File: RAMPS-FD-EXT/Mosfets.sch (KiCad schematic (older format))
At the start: 30 parts, among them P301 FET_1, P302 FET_0, P303 FET_3, P304 FET_2, Q301 2N7002, Q302 2N7002, Q303 IRLB8743PBF, Q304 IRLB8743PBF, Q305 2N7002, Q306 2N7002, Q307 IRLB8743PBF, Q308 IRLB8743PBF

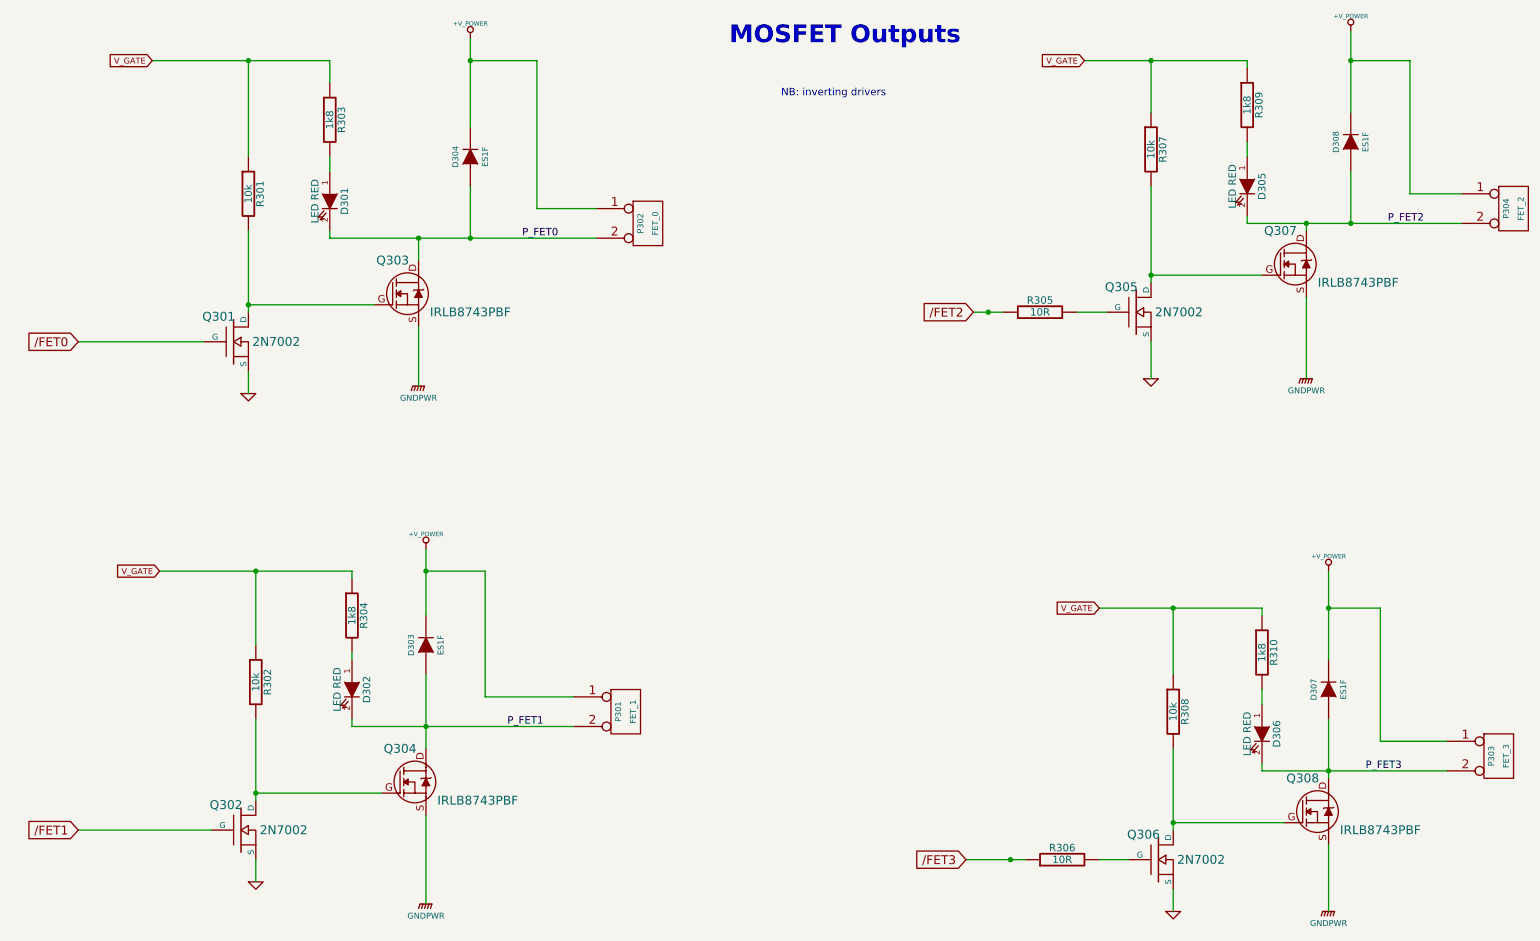
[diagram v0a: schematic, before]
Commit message: EXT4: update schematic, layout
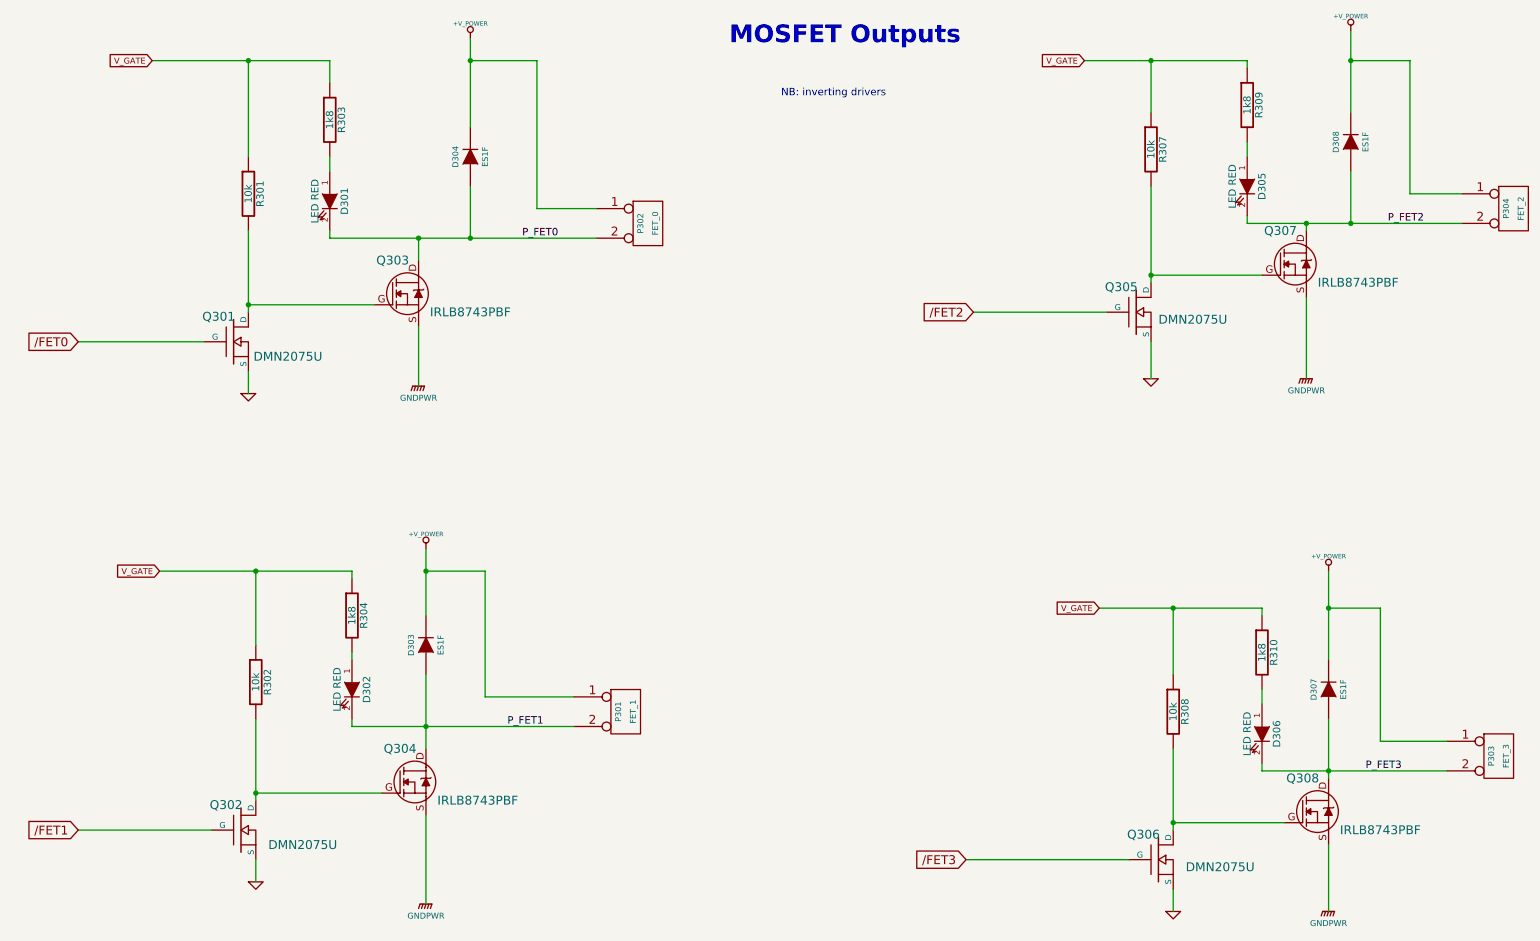
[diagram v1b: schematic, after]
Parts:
- removed R305, R306: 10R, symbol R
- Q301, Q302, Q305, Q306: value 2N7002 -> DMN2075U
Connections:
- net /FET2: now also Q305.G
- net /FET3: now also Q306.G
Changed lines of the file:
@@
 Sheet 3 4
 Title ""
-Date "21 sep 2013"
+Date "26 sep 2013"
 Rev ""
 Comp ""
@@
 $EndDescr
 $Comp
-L GNDPWR #PWR042
+L GNDPWR #PWR046
 U 1 1 523B8B99
 P 3500 3050
-F 0 "#PWR042" H 3500 3100 40  0001 C CNN
+F 0 "#PWR046" H 3500 3100 40  0001 C CNN
 F 1 "GNDPWR" H 3500 2970 40  0000 C CNN
 F 2 "" H 3500 3050 60  0001 C CNN
@@
 $EndComp
 $Comp
-L +V_POWER #PWR043
+L +V_POWER #PWR047
 U 1 1 523B8B8F
 P 3850 700
-F 0 "#PWR043" H 3850 670 30  0001 C CNN
+F 0 "#PWR047" H 3850 670 30  0001 C CNN
 F 1 "+V_POWER" H 3850 800 30  0000 C CNN
 F 2 "" H 3850 700 60  0001 C CNN
@@
 	1    0    0    -1
 $EndComp
-$Comp
-L R R306
-U 1 1 523B8B8A
-P 7850 6250
-F 0 "R306" V 7930 6250 50  0000 C CNN
-F 1 "10R" V 7850 6250 50  0000 C CNN
-F 2 "" H 7850 6250 60  0001 C CNN
-F 3 "" H 7850 6250 60  0001 C CNN
-	1    7850 6250
-	0    -1   -1   0
-$EndComp
 Text GLabel 1200 6050 0    60   Input ~ 0
 /FET1
@@
 P 8500 6250
 F 0 "Q306" H 8510 6420 60  0000 R CNN
-F 1 "2N7002" H 8950 6250 60  0000 R CNN
+F 1 "DMN2075U" H 9150 6200 60  0000 R CNN
 F 2 "" H 8500 6250 60  0001 C CNN
 F 3 "" H 8500 6250 60  0001 C CNN
@@
 $EndComp
 $Comp
-L +V_POWER #PWR044
+L +V_POWER #PWR048
 U 1 1 523B8B82
 P 9650 4300
-F 0 "#PWR044" H 9650 4270 30  0001 C CNN
+F 0 "#PWR048" H 9650 4270 30  0001 C CNN
 F 1 "+V_POWER" H 9650 4400 30  0000 C CNN
 F 2 "" H 9650 4300 60  0001 C CNN
@@
 $EndComp
 $Comp
-L +V_POWER #PWR045
+L +V_POWER #PWR049
 U 1 1 523B8B81
 P 3550 4150
-F 0 "#PWR045" H 3550 4120 30  0001 C CNN
+F 0 "#PWR049" H 3550 4120 30  0001 C CNN
 F 1 "+V_POWER" H 3550 4250 30  0000 C CNN
 F 2 "" H 3550 4150 60  0001 C CNN
@@
 $EndComp
 $Comp
-L +V_POWER #PWR046
+L +V_POWER #PWR050
 U 1 1 523B8B7F
 P 9800 650
-F 0 "#PWR046" H 9800 620 30  0001 C CNN
+F 0 "#PWR050" H 9800 620 30  0001 C CNN
 F 1 "+V_POWER" H 9800 750 30  0000 C CNN
 F 2 "" H 9800 650 60  0001 C CNN
@@
 P 8350 2550
 F 0 "Q305" H 8360 2720 60  0000 R CNN
-F 1 "2N7002" H 8800 2550 60  0000 R CNN
+F 1 "DMN2075U" H 8500 2500 60  0000 L CNN
 F 2 "" H 8350 2550 60  0001 C CNN
 F 3 "" H 8350 2550 60  0001 C CNN
@@
 /FET2
 $Comp
-L R R305
-U 1 1 523B8B7B
-P 7700 2550
-F 0 "R305" V 7780 2550 50  0000 C CNN
-F 1 "10R" V 7700 2550 50  0000 C CNN
-F 2 "" H 7700 2550 60  0001 C CNN
-F 3 "" H 7700 2550 60  0001 C CNN
-	1    7700 2550
-	0    -1   -1   0
-$EndComp
-$Comp
-L GND #PWR047
+L GND #PWR051
 U 1 1 523B8B7A
 P 8450 3000
-F 0 "#PWR047" H 8450 3000 30  0001 C CNN
+F 0 "#PWR051" H 8450 3000 30  0001 C CNN
 F 1 "GND" H 8450 2930 30  0001 C CNN
 F 2 "" H 8450 3000 60  0001 C CNN
@@
 $EndComp
 $Comp
-L GNDPWR #PWR048
+L GNDPWR #PWR052
 U 1 1 523B8B6F
 P 3550 6550
-F 0 "#PWR048" H 3550 6600 40  0001 C CNN
+F 0 "#PWR052" H 3550 6600 40  0001 C CNN
 F 1 "GNDPWR" H 3550 6470 40  0000 C CNN
 F 2 "" H 3550 6550 60  0001 C CNN
@@
 $EndComp
 $Comp
-L GNDPWR #PWR049
+L GNDPWR #PWR053
 U 1 1 523B8B6E
 P 9650 6600
-F 0 "#PWR049" H 9650 6650 40  0001 C CNN
+F 0 "#PWR053" H 9650 6650 40  0001 C CNN
 F 1 "GNDPWR" H 9650 6520 40  0000 C CNN
 F 2 "" H 9650 6600 60  0001 C CNN
@@
 $EndComp
 $Comp
-L GND #PWR050
+L GND #PWR054
 U 1 1 523B8B6D
 P 8600 6600
-F 0 "#PWR050" H 8600 6600 30  0001 C CNN
+F 0 "#PWR054" H 8600 6600 30  0001 C CNN
 F 1 "GND" H 8600 6530 30  0001 C CNN
 F 2 "" H 8600 6600 60  0001 C CNN
@@
 $EndComp
 $Comp
-L GNDPWR #PWR051
+L GNDPWR #PWR055
 U 1 1 523B8B6C
 P 9500 3000
-F 0 "#PWR051" H 9500 3050 40  0001 C CNN
+F 0 "#PWR055" H 9500 3050 40  0001 C CNN
 F 1 "GNDPWR" H 9500 2920 40  0000 C CNN
 F 2 "" H 9500 3000 60  0001 C CNN
@@
 $EndComp
 $Comp
-L GND #PWR052
+L GND #PWR056
 U 1 1 523B8B6B
 P 2400 6400
-F 0 "#PWR052" H 2400 6400 30  0001 C CNN
+F 0 "#PWR056" H 2400 6400 30  0001 C CNN
 F 1 "GND" H 2400 6330 30  0001 C CNN
 F 2 "" H 2400 6400 60  0001 C CNN
@@
 P 2300 6050
 F 0 "Q302" H 2310 6220 60  0000 R CNN
-F 1 "2N7002" H 2750 6050 60  0000 R CNN
+F 1 "DMN2075U" H 2950 5950 60  0000 R CNN
 F 2 "" H 2300 6050 60  0001 C CNN
 F 3 "" H 2300 6050 60  0001 C CNN
@@
 P 2250 2750
 F 0 "Q301" H 2260 2920 60  0000 R CNN
-F 1 "2N7002" H 2700 2750 60  0000 R CNN
+F 1 "DMN2075U" H 2850 2650 60  0000 R CNN
 F 2 "" H 2250 2750 60  0001 C CNN
 F 3 "" H 2250 2750 60  0001 C CNN
@@
 $EndComp
 $Comp
-L GND #PWR053
+L GND #PWR057
 U 1 1 523B8B66
 P 2350 3100
-F 0 "#PWR053" H 2350 3100 30  0001 C CNN
+F 0 "#PWR057" H 2350 3100 30  0001 C CNN
 F 1 "GND" H 2350 3030 30  0001 C CNN
 F 2 "" H 2350 3100 60  0001 C CNN
@@
 V_GATE
 Wire Wire Line
-	3550 4600 3550 4150
+	3550 4150 3550 4600
 Wire Wire Line
 	2100 6050 1200 6050
@@
 	2400 6400 2400 6250
 Wire Wire Line
-	2400 5850 2400 5300
+	2400 5300 2400 5850
 Wire Wire Line
 	3250 5800 2400 5800
@@
 	9200 5650 10450 5650
 Wire Wire Line
-	9200 4600 9200 4550
+	9200 4550 9200 4600
 Wire Wire Line
 	9650 4300 9650 4900
@@
 	3950 5150 4550 5150
 Wire Wire Line
-	3850 1300 3850 700
+	3850 700  3850 1300
 Wire Wire Line
 	1700 850  2900 850
@@
 	2900 2050 4700 2050
 Wire Wire Line
-	3050 4350 3050 4300
+	3050 4300 3050 4350
 Wire Wire Line
 	3550 5000 3550 5500
@@
 Connection ~ 9800 850
 Wire Wire Line
-	9800 1200 9800 650
+	9800 650  9800 1200
 Wire Wire Line
 	10200 1750 10200 850
@@
 	9200 2300 8450 2300
 Wire Wire Line
-	8450 2350 8450 1700
-Wire Wire Line
-	8150 2550 7950 2550
+	8450 1700 8450 2350
+Wire Wire Line
+	8150 2550 7250 2550
 Wire Wire Line
 	9100 1500 9100 1400
-Wire Wire Line
-	7250 2550 7450 2550
 Wire Wire Line
 	8450 1200 8450 850
@@
 	2900 1600 2900 1500
 Wire Wire Line
-	7200 6250 7600 6250
-Wire Wire Line
 	9200 5200 9200 5100
-Wire Wire Line
-	8300 6250 8100 6250
 Wire Wire Line
 	8600 5500 8600 6050
@@
 Wire Wire Line
 	4300 1850 4700 1850
-Connection ~ 7500 6250
-Connection ~ 7350 2550
 Wire Wire Line
 	9800 1600 9800 1950
@@
 	3050 5350 4550 5350
 Wire Wire Line
-	3050 4300 1750 4300
-Wire Wire Line
-	9650 5700 9650 5300
+	1750 4300 3050 4300
+Wire Wire Line
+	9650 5300 9650 5700
 Wire Wire Line
 	10450 5450 10000 5450
@@
 Connection ~ 9650 4550
 Wire Wire Line
-	9200 4550 8100 4550
+	8100 4550 9200 4550
 Connection ~ 8600 4550
 Wire Wire Line
@@
 	3200 2500 2350 2500
 Wire Wire Line
-	2350 2550 2350 2000
+	2350 2000 2350 2550
 Wire Wire Line
 	2350 3100 2350 2950
@@
 Text Label 9900 5650 0    50   ~ 0
 P_FET3
+Wire Wire Line
+	8300 6250 7200 6250
 $EndSCHEMATC

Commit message: RAMPS-FD V2.A
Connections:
- net +V_POWER: now also R303.1, R304.1, R309.1, R310.1
- net V_GATE: no longer R303.1, R304.1, R309.1, R310.1
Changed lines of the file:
@@
 Sheet 3 6
 Title ""
-Date "10 oct 2013"
+Date "8 feb 2014"
 Rev ""
 Comp ""
@@
 Text GLabel 1750 4300 0    40   Input ~ 0
 V_GATE
-Wire Wire Line
-	3550 4150 3550 4600
-Wire Wire Line
-	2100 6050 1200 6050
-Connection ~ 2350 850
-Wire Wire Line
-	2350 850  2350 1500
-Connection ~ 2400 5800
-Wire Wire Line
-	2400 6400 2400 6250
-Wire Wire Line
-	2400 5300 2400 5850
-Wire Wire Line
-	3250 5800 2400 5800
-Wire Wire Line
-	9500 3000 9500 2450
-Connection ~ 8450 850
-Wire Wire Line
-	8000 850  9100 850
-Wire Wire Line
-	9100 1900 9100 1950
-Wire Wire Line
-	9100 1950 10550 1950
-Wire Wire Line
-	9200 5600 9200 5650
-Wire Wire Line
-	9200 5650 10450 5650
-Wire Wire Line
-	9200 4550 9200 4600
-Wire Wire Line
-	9650 4300 9650 4900
-Wire Wire Line
-	3950 5150 3950 4300
-Wire Wire Line
-	3950 5150 4550 5150
-Wire Wire Line
-	3850 700  3850 1300
-Wire Wire Line
-	1700 850  2900 850
-Wire Wire Line
-	2900 2000 2900 2050
-Wire Wire Line
-	2900 2050 4700 2050
-Wire Wire Line
-	3050 4300 3050 4350
-Wire Wire Line
-	3550 5000 3550 5500
-Connection ~ 3850 850
-Connection ~ 9800 850
-Wire Wire Line
-	9800 650  9800 1200
-Wire Wire Line
-	10200 1750 10200 850
-Wire Wire Line
-	10200 1750 10550 1750
-Wire Wire Line
-	9100 850  9100 900
-Connection ~ 8450 2300
-Wire Wire Line
-	9200 2300 8450 2300
-Wire Wire Line
-	8450 1700 8450 2350
-Wire Wire Line
-	8150 2550 7250 2550
-Wire Wire Line
-	9100 1500 9100 1400
-Wire Wire Line
-	8450 1200 8450 850
-Connection ~ 9650 5650
-Connection ~ 3500 2050
-Wire Wire Line
-	3500 2050 3500 2200
-Connection ~ 3550 5350
-Wire Wire Line
-	9650 6150 9650 6600
-Wire Wire Line
-	3500 2650 3500 3050
-Wire Wire Line
-	8600 5000 8600 4550
-Wire Wire Line
-	3050 4900 3050 4850
-Wire Wire Line
-	2900 1600 2900 1500
-Wire Wire Line
-	9200 5200 9200 5100
-Wire Wire Line
-	8600 5500 8600 6050
-Wire Wire Line
-	8600 6600 8600 6450
-Wire Wire Line
-	9350 6000 8600 6000
-Connection ~ 8600 6000
-Wire Wire Line
-	4300 1850 4300 850
-Wire Wire Line
-	4300 1850 4700 1850
-Wire Wire Line
-	9800 1600 9800 1950
-Connection ~ 9800 1950
-Wire Wire Line
-	3850 1700 3850 2050
-Connection ~ 3850 2050
-Wire Wire Line
-	3050 5300 3050 5350
-Wire Wire Line
-	2900 850  2900 1000
-Wire Wire Line
-	3050 5350 4550 5350
-Wire Wire Line
-	1750 4300 3050 4300
-Wire Wire Line
-	9650 5300 9650 5700
-Wire Wire Line
-	10450 5450 10000 5450
-Wire Wire Line
-	10000 5450 10000 4550
-Wire Wire Line
-	10000 4550 9650 4550
-Connection ~ 9650 4550
-Wire Wire Line
-	8100 4550 9200 4550
-Connection ~ 8600 4550
-Wire Wire Line
-	3550 6550 3550 5950
-Wire Wire Line
-	9500 1950 9500 2000
-Connection ~ 9500 1950
-Wire Wire Line
-	10200 850  9800 850
-Wire Wire Line
-	8450 3000 8450 2750
-Wire Wire Line
-	2400 4800 2400 4300
-Connection ~ 2400 4300
-Wire Wire Line
-	3200 2500 2350 2500
-Wire Wire Line
-	2350 2000 2350 2550
-Wire Wire Line
-	2350 3100 2350 2950
-Connection ~ 2350 2500
-Wire Wire Line
-	1200 2750 2050 2750
-Wire Wire Line
-	4300 850  3850 850
-Wire Wire Line
-	3950 4300 3550 4300
-Connection ~ 3550 4300
 Text GLabel 8100 4550 0    40   Input ~ 0
 V_GATE
@@
 P_FET3
 Wire Wire Line
+	3550 4150 3550 4600
+Wire Wire Line
+	2100 6050 1200 6050
+Connection ~ 2350 850
+Wire Wire Line
+	2350 850  2350 1500
+Connection ~ 2400 5800
+Wire Wire Line
+	2400 6400 2400 6250
+Wire Wire Line
+	2400 5300 2400 5850
+Wire Wire Line
+	3250 5800 2400 5800
+Wire Wire Line
+	9500 3000 9500 2450
+Connection ~ 8450 850
+Wire Wire Line
+	9100 1900 9100 1950
+Wire Wire Line
+	9100 1950 10550 1950
+Wire Wire Line
+	9200 5600 9200 5650
+Wire Wire Line
+	9200 5650 10450 5650
+Wire Wire Line
+	9200 4550 9200 4600
+Wire Wire Line
+	9650 4300 9650 4900
+Wire Wire Line
+	3950 4300 3950 5150
+Wire Wire Line
+	3950 5150 4550 5150
+Wire Wire Line
+	3850 700  3850 1300
+Wire Wire Line
+	2900 2000 2900 2050
+Wire Wire Line
+	2900 2050 4700 2050
+Wire Wire Line
+	3050 4300 3050 4350
+Wire Wire Line
+	3550 5000 3550 5500
+Connection ~ 3850 850
+Connection ~ 9800 850
+Wire Wire Line
+	9800 650  9800 1200
+Wire Wire Line
+	10200 850  10200 1750
+Wire Wire Line
+	10200 1750 10550 1750
+Wire Wire Line
+	9100 850  9100 900
+Connection ~ 8450 2300
+Wire Wire Line
+	9200 2300 8450 2300
+Wire Wire Line
+	8450 1700 8450 2350
+Wire Wire Line
+	8150 2550 7250 2550
+Wire Wire Line
+	9100 1500 9100 1400
+Wire Wire Line
+	8450 1200 8450 850
+Connection ~ 9650 5650
+Connection ~ 3500 2050
+Wire Wire Line
+	3500 2050 3500 2200
+Connection ~ 3550 5350
+Wire Wire Line
+	9650 6150 9650 6600
+Wire Wire Line
+	3500 2650 3500 3050
+Wire Wire Line
+	8600 5000 8600 4550
+Wire Wire Line
+	3050 4900 3050 4850
+Wire Wire Line
+	2900 1600 2900 1500
+Wire Wire Line
+	9200 5200 9200 5100
+Wire Wire Line
+	8600 5500 8600 6050
+Wire Wire Line
+	8600 6600 8600 6450
+Wire Wire Line
+	9350 6000 8600 6000
+Connection ~ 8600 6000
+Wire Wire Line
+	4300 850  4300 1850
+Wire Wire Line
+	4300 1850 4700 1850
+Wire Wire Line
+	9800 1600 9800 1950
+Connection ~ 9800 1950
+Wire Wire Line
+	3850 1700 3850 2050
+Connection ~ 3850 2050
+Wire Wire Line
+	3050 5300 3050 5350
+Wire Wire Line
+	2900 850  2900 1000
+Wire Wire Line
+	3050 5350 4550 5350
+Wire Wire Line
+	9650 5300 9650 5700
+Wire Wire Line
+	10450 5450 10000 5450
+Wire Wire Line
+	10000 5450 10000 4550
+Wire Wire Line
+	10000 4550 9200 4550
+Connection ~ 9650 4550
+Connection ~ 8600 4550
+Wire Wire Line
+	3550 6550 3550 5950
+Wire Wire Line
+	9500 1950 9500 2000
+Connection ~ 9500 1950
+Wire Wire Line
+	9100 850  10200 850
+Wire Wire Line
+	8450 3000 8450 2750
+Wire Wire Line
+	2400 4800 2400 4300
+Connection ~ 2400 4300
+Wire Wire Line
+	3200 2500 2350 2500
+Wire Wire Line
+	2350 2000 2350 2550
+Wire Wire Line
+	2350 3100 2350 2950
+Connection ~ 2350 2500
+Wire Wire Line
+	1200 2750 2050 2750
+Wire Wire Line
+	2900 850  4300 850
+Wire Wire Line
+	3050 4300 3950 4300
+Connection ~ 3550 4300
+Wire Wire Line
 	8300 6250 7200 6250
+Wire Wire Line
+	2350 850  1700 850
+Wire Wire Line
+	8450 850  8000 850
+Wire Wire Line
+	2400 4300 1750 4300
+Wire Wire Line
+	8600 4550 8100 4550
 $EndSCHEMATC
